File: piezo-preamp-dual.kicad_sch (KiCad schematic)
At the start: 37 parts, among them J1 piezo, J2 piezo, J3 piezo, J4 piezo, J5 output, J6 Conn_01x03_Pin, J7 AudioJack, U1 OPA1677, U2 OPA1677, U3 OPA1677

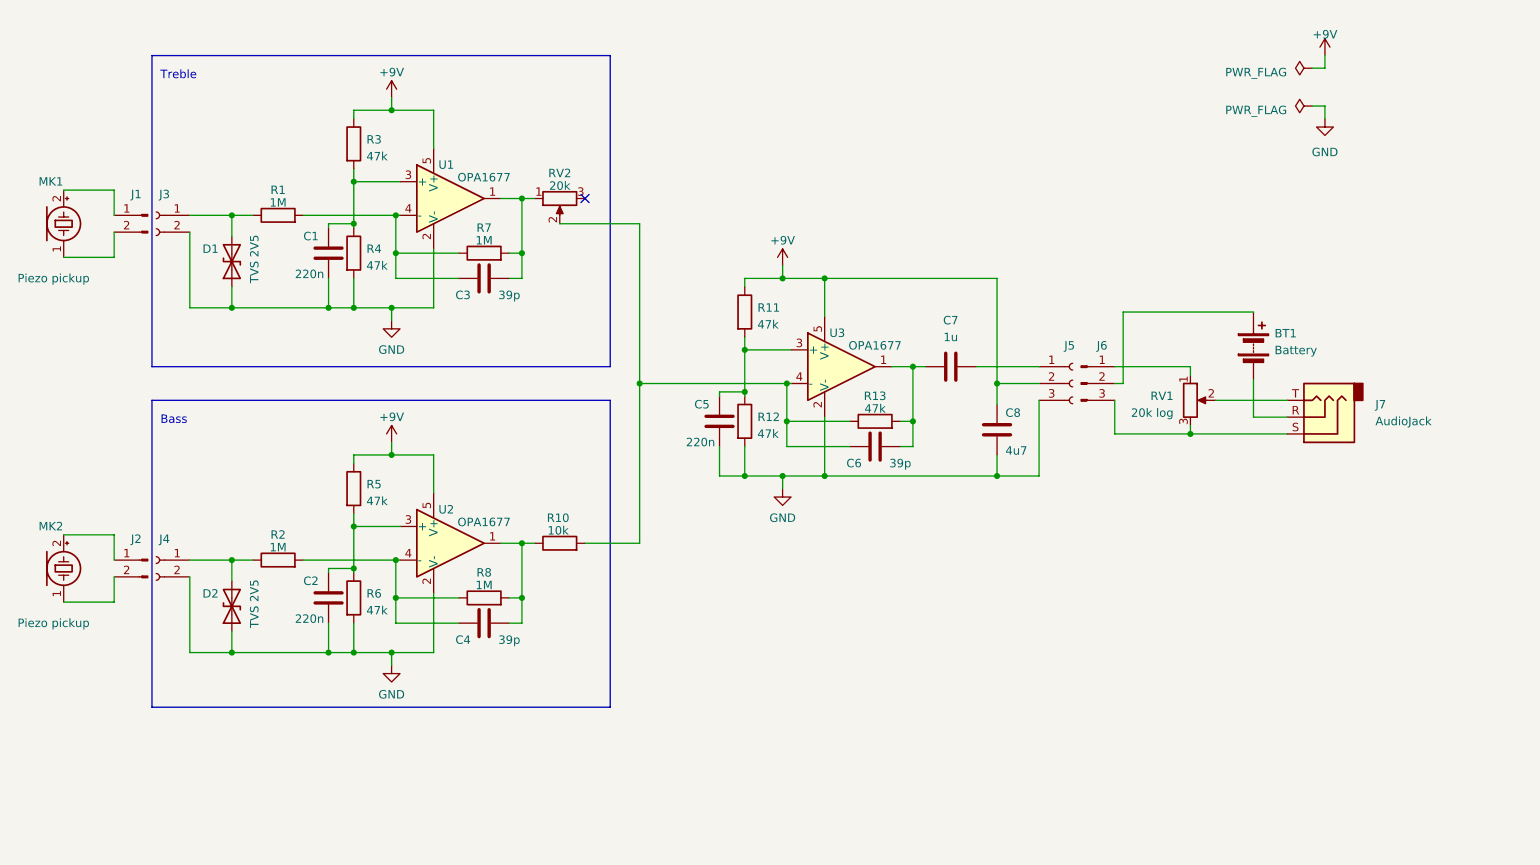
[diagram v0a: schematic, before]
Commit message: The TVS diodes were removed from the "dual-channel" design. The PCB is slighly smaller as a result.
The parasitic capacitance of the TVS diodes had a negative effect on the sound. In addition, they were redundant; the inputs of the OPA1677 are already protected against overvoltage, so the 1 MOhm resistor is ample protection.

Signed-off-by: Thiadmer Riemersma <thiadmer@compuphase.com>
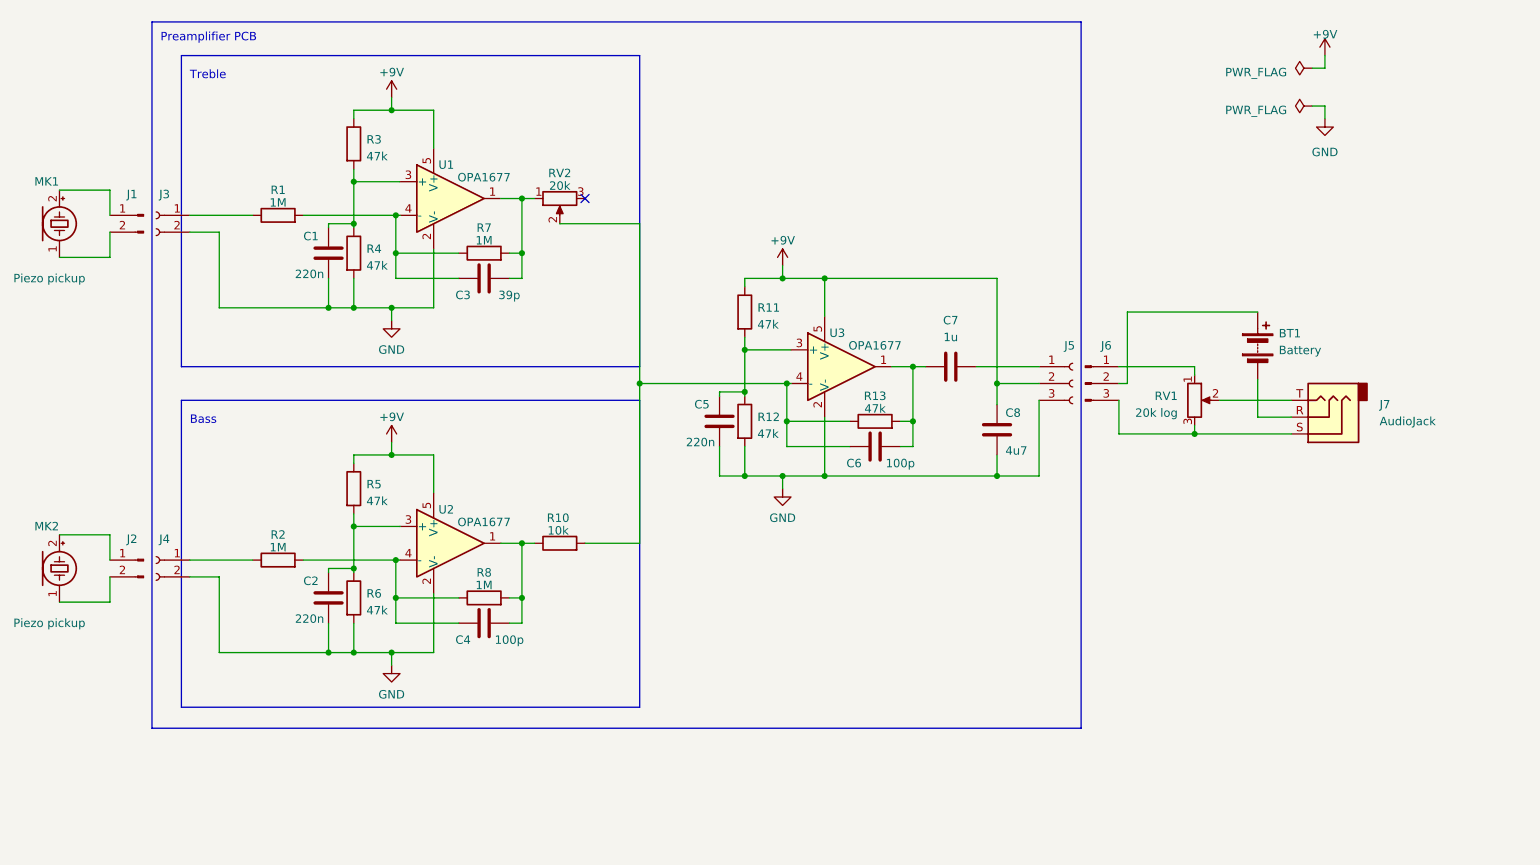
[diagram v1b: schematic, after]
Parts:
- removed D1, D2: TVS 2V5, VisualPlace:SOD523, symbol Device:D_TVS
- C4, C6: value 39p -> 100p
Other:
- note added: "Preamplifier PCB"
- moved on the sheet: BT1, J1, J2, J6, J7, MK1, MK2, RV1

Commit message: Added bass-boost filter (dual-channel preamp only). Added Bill-Of-Materials file. Fixed PDF of the schematic (turned out to be unreadable).
Signed-off-by: Thiadmer Riemersma <thiadmer@compuphase.com>
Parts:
- removed J7: AudioJack, symbol Connector_Audio:AudioJack3
- removed R10: 10k, VisualPlace:0603, symbol Device:R
- added J7: N113X, symbol Connect_Audio:N113X
- added R9: 47k, VisualPlace:0603, symbol Device:R
- C3: value 39p -> 68p
- C4: value 100p -> 68p
- C6: value 100p -> 10n
- R11, R12, R13, R3, R4, R5, R6: value 47k -> 68k
- RV2: ProductNumber (none) -> 3312J-1-203E
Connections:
- net at BT1.1 (+): now also J7.3 (SW1); no longer J6.2 (Pin_2)
- net at J6.3 (Pin_3), RV1.3: now also BT1.2 (-), J7.1 (Tip)
- net at C6.2, C7.1, U3.1: now also R9.2; no longer R13.2
- net at R13.1, RV2.2, U3.4 (-): no longer C6.1
- net at RV1.2: now also J7.1 (Tip)
- net at C4.2, R8.2, U2.1: now also RV2.3
- new net: J6.2 (Pin_2), J7.4 (SW2)
- new net: C6.1, R13.2, R9.1
- no-connect marks 1 -> 0
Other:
- title: Piezo-pickup impedance converter, split pickup -> Piezo-pickup impedance converter, split pickup, bass boost
- moved on the sheet: BT1, C6, C7, C8, J5, J6, R13, RV1, RV2

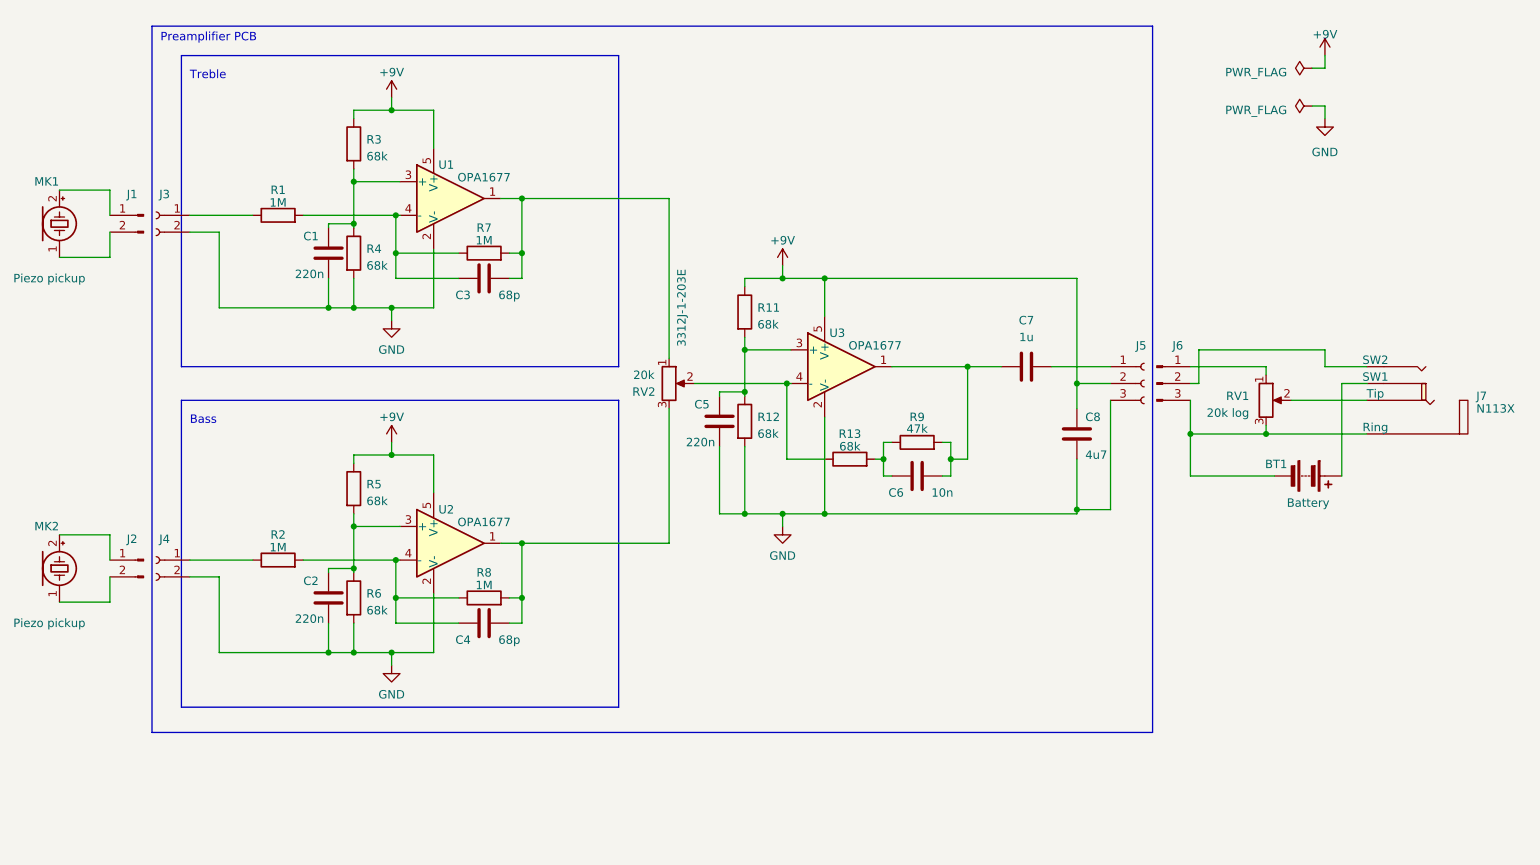
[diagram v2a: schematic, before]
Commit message: Reduce (peak) voltage of the piezo pick-ups, to avoid saturatating the opamps. Switch opamps to OPA323, to avoid clamping diodes on input. Higher input impedance.
Signed-off-by: thiadmer <thiadmer.riemersma@gmail.com>
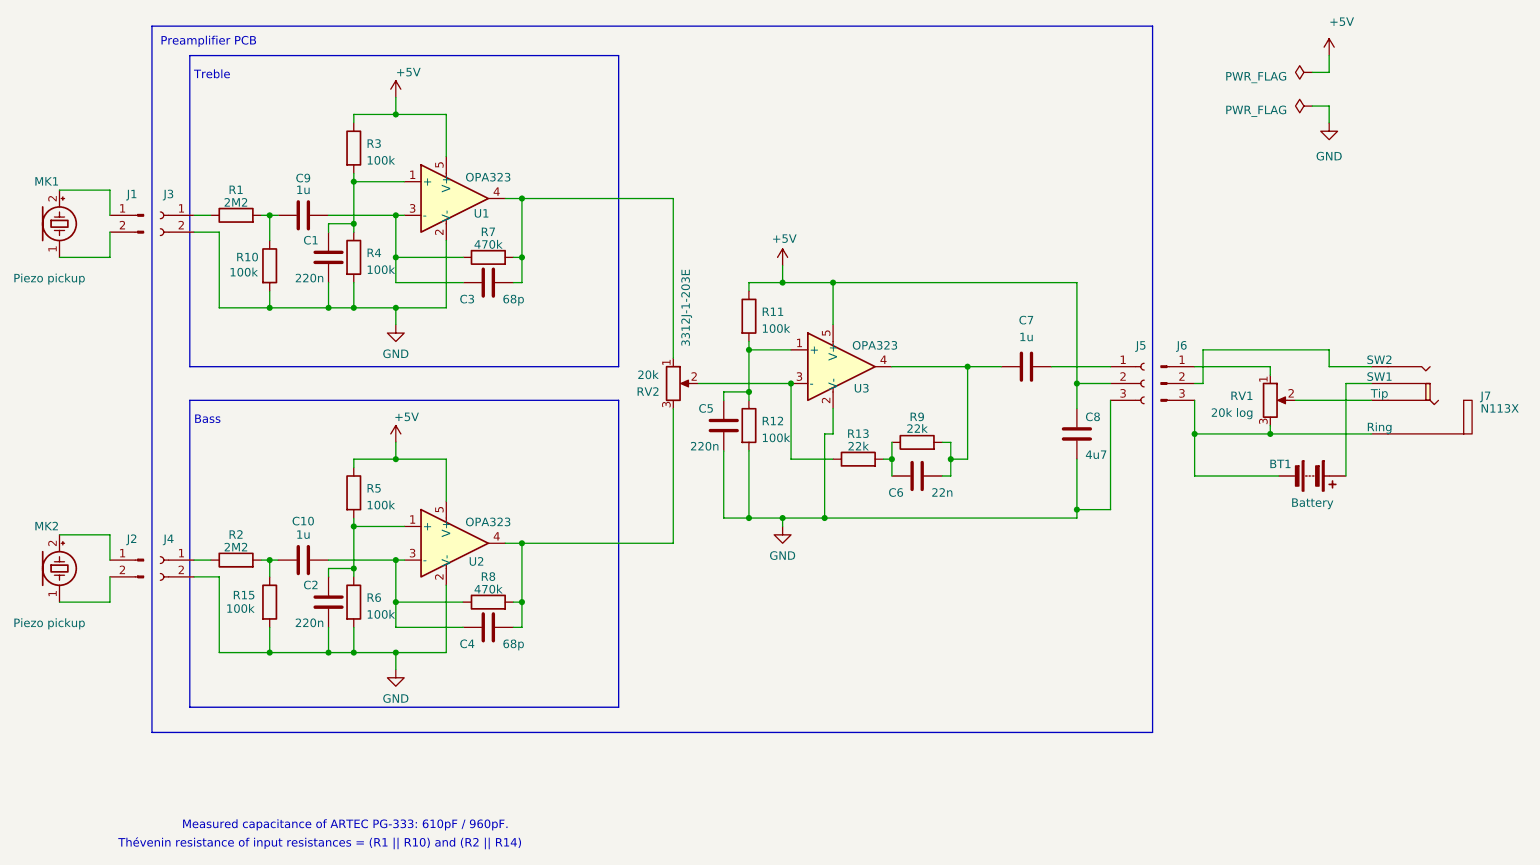
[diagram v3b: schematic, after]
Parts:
- added C10, C9: 1u, symbol Device:C
- added R10, R15: 100k, VisualPlace:0603, symbol Device:R
- C6: value 10n -> 22n
- R1, R2: value 1M -> 2M2
- R11, R12, R3, R4, R5, R6: value 68k -> 100k
- R13: value 68k -> 22k
- R7, R8: value 1M -> 470k
- R9: value 47k -> 22k
- U1, U2, U3: value OPA1677 -> OPA323; footprint VisualPlace:SOT23-5 -> VisualPlace:SOT353; symbol Amplifier_Operational:OPA1677DBV -> Analogue_Devices:OPA323DCK
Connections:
- net GND: now also R10.2, R15.2
- net at C1.1, R3.2, R4.1: now also U1.1 (+); no longer U1.3 (+)
- net at C3.2, R7.2, RV2.1: now also U1.4; no longer U1.1
- net at C3.1, R7.1: now also U1.3 (-), C9.2; no longer R1.2, U1.4 (-)
- net at C2.1, R5.2, R6.1: now also U2.1 (+); no longer U2.3 (+)
- net at C5.1, R11.2, R12.1: now also U3.1 (+); no longer U3.3 (+)
- net at C6.2, C7.1, R9.2: now also U3.4; no longer U3.1
- net at R13.1, RV2.2: now also U3.3 (-); no longer U3.4 (-)
- net at C4.1, R8.1: now also U2.3 (-), C10.2; no longer R2.2, U2.4 (-)
- net at C4.2, R8.2, RV2.3: now also U2.4; no longer U2.1
- net +9V renamed +5V
- new net: C10.1, R15.1, R2.2
- new net: C9.1, R1.2, R10.1
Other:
- note added: "Measured capacitance of ARTEC PG-333: 610pF / 960pF."
- note added: "Thévenin resistance of input resistances = (R1 || R10) and (R2 || R14)"
- moved on the sheet: BT1, C1, C2, C3, C4, C5, J3, J4, J6, J7, R1, R11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
